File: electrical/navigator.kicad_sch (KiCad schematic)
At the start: 7 parts

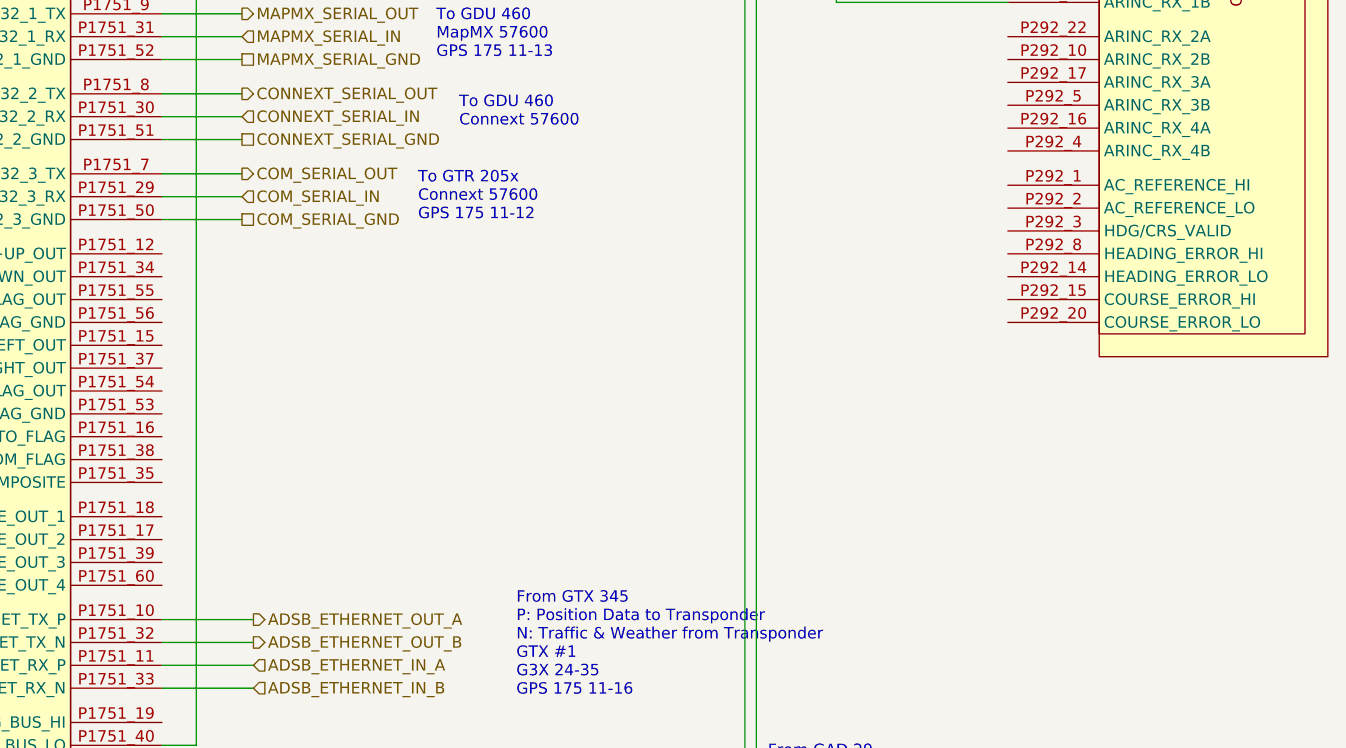
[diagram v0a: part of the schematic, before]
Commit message: Changed GPS 175 to not have connection to GTS 205x per g3xpert. Moved ELT GPS from GPS 175 and used RS-232 on GDU 460 for GEA 24 backup.
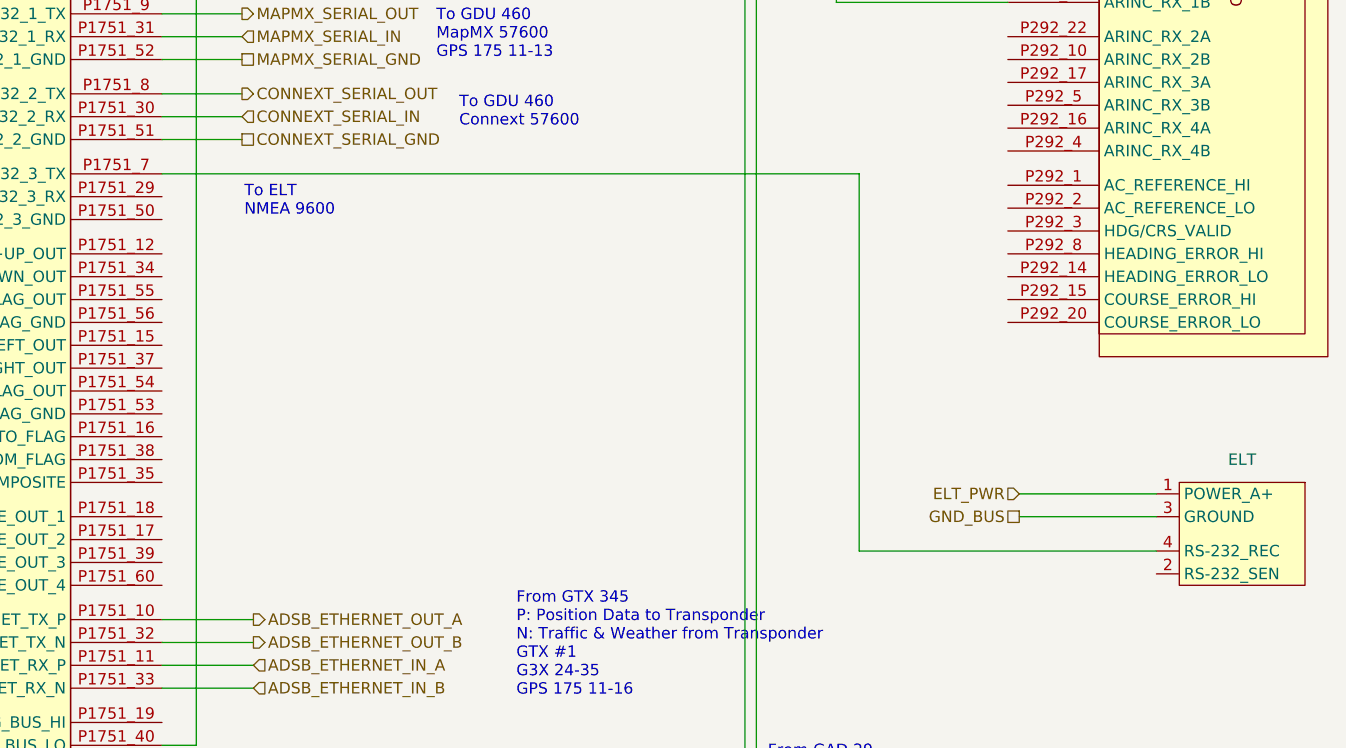
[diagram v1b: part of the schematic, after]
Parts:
- added ELT: ~, symbol flyerx:ACK_E-04
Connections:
- net GND: now also ELT.3 (GROUND)
- net COM_SERIAL_GND: no longer names the net of GPS175.P1751_50 (RS-232_3_GND)
- net COM_SERIAL_IN: no longer names the net of GPS175.P1751_29 (RS-232_3_RX)
- net COM_SERIAL_OUT: no longer names the net of GPS175.P1751_7 (RS-232_3_TX)
- net COM_SERIAL_OUT: now also ELT.4 (RS-232_REC)
- new net ELT_PWR: ELT.1 (POWER_A+)
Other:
- note added: "To ELT NMEA 9600"
- note removed: "To GTR 205x Connext 57600 GPS 175 11-12"
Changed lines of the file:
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@@
 	(paper "USLetter" portrait)
 	(title_block
-		(date "2025-09-08")
-		(rev "1.0")
+		(date "2025-09-09")
+		(rev "1.0.1")
 		(company "N78HR")
 	)
@@
 		)
 	)
+	(text "To ELT\nNMEA 9600"
+		(exclude_from_sim no)
+		(at 73.914 97.536 0)
+		(effects
+			(font
+				(size 1.27 1.27)
+			)
+			(justify left bottom)
+		)
+	)
 	(text "From GAD 29\nEFIS/AirData Low Gama Format 1\nG3X 24-38\nGPS 175 11-13"
 		(exclude_from_sim no)
 		(at 132.08 163.83 0)
-		(effects
-			(font
-				(size 1.27 1.27)
-			)
-			(justify left bottom)
-		)
-	)
-	(text "To GTR 205x\nConnext 57600\nGPS 175 11-12"
-		(exclude_from_sim no)
-		(at 93.218 98.044 0)
 		(effects
 			(font
@@
 	(wire
 		(pts
-			(xy 64.77 92.71) (xy 73.66 92.71)
-		)
-		(stroke
-			(width 0)
-			(type default)
-		)
-	)
-	(wire
-		(pts
 			(xy 64.77 156.21) (xy 68.58 156.21)
 		)
@@
 	(wire
 		(pts
+			(xy 64.77 92.71) (xy 142.24 92.71)
+		)
+		(stroke
+			(width 0)
+			(type default)
+		)
+	)
+	(wire
+		(pts
 			(xy 129.54 43.18) (xy 152.4 43.18)
 		)
@@
 	(wire
 		(pts
+			(xy 160.02 130.81) (xy 175.26 130.81)
+		)
+		(stroke
+			(width 0)
+			(type default)
+		)
+	)
+	(wire
+		(pts
 			(xy 31.75 260.35) (xy 36.83 260.35)
 		)
@@
 	(wire
 		(pts
+			(xy 160.02 128.27) (xy 175.26 128.27)
+		)
+		(stroke
+			(width 0)
+			(type default)
+		)
+	)
+	(wire
+		(pts
 			(xy 129.54 160.02) (xy 129.54 48.26)
 		)
@@
 	(wire
 		(pts
-			(xy 64.77 95.25) (xy 73.66 95.25)
-		)
-		(stroke
-			(width 0)
-			(type default)
-		)
-	)
-	(wire
-		(pts
 			(xy 64.77 77.47) (xy 73.66 77.47)
 		)
@@
 	(wire
 		(pts
+			(xy 142.24 134.62) (xy 175.26 134.62)
+		)
+		(stroke
+			(width 0)
+			(type default)
+		)
+	)
+	(wire
+		(pts
 			(xy 68.58 29.21) (xy 68.58 26.67)
 		)
@@
 	(wire
 		(pts
-			(xy 64.77 97.79) (xy 73.66 97.79)
-		)
-		(stroke
-			(width 0)
-			(type default)
-		)
-	)
-	(wire
-		(pts
 			(xy 64.77 74.93) (xy 73.66 74.93)
 		)
@@
 		(pts
 			(xy 64.77 144.78) (xy 74.93 144.78)
+		)
+		(stroke
+			(width 0)
+			(type default)
+		)
+	)
+	(wire
+		(pts
+			(xy 142.24 92.71) (xy 142.24 134.62)
 		)
 		(stroke
@@
 		)
 	)
+	(hierarchical_label "ELT_PWR"
+		(shape input)
+		(at 160.02 128.27 180)
+		(effects
+			(font
+				(size 1.27 1.27)
+			)
+			(justify right)
+		)
+	)
 	(hierarchical_label "CAN_LO_OUT"
 		(shape output)
@@
 		)
 	)
-	(hierarchical_label "COM_SERIAL_IN"
-		(shape input)
-		(at 73.66 95.25 0)
-		(effects
-			(font
-				(size 1.27 1.27)
-			)
-			(justify left)
-		)
-	)
-	(hierarchical_label "COM_SERIAL_GND"
-		(shape passive)
-		(at 73.66 97.79 0)
-		(effects
-			(font
-				(size 1.27 1.27)
-			)
-			(justify left)
-		)
-	)
 	(hierarchical_label "CAN_HI_IN"
 		(shape input)
@@
 		)
 	)
-	(hierarchical_label "COM_SERIAL_OUT"
-		(shape output)
-		(at 73.66 92.71 0)
-		(effects
-			(font
-				(size 1.27 1.27)
-			)
-			(justify left)
+	(hierarchical_label "GND_BUS"
+		(shape passive)
+		(at 160.02 130.81 180)
+		(effects
+			(font
+				(size 1.27 1.27)
+			)
+			(justify right)
 		)
 	)
@@
 					(unit 1)
 				)
+			)
+		)
+	)
+	(symbol
+		(lib_id "flyerx:ACK_E-04")
+		(at 191.77 127 0)
+		(mirror y)
+		(unit 1)
+		(exclude_from_sim no)
+		(in_bom yes)
+		(on_board yes)
+		(dnp no)
+		(property "Reference" "ELT"
+			(at 184.785 124.46 0)
+			(effects
+				(font
+					(size 1.27 1.27)
+				)
+			)
+		)
+		(property "Value" "~"
+			(at 191.77 125.73 0)
+			(effects
+				(font
+					(size 1.27 1.27)
+				)
+			)
+		)
+		(property "Footprint" ""
+			(at 191.77 125.73 0)
+			(effects
+				(font
+					(size 1.27 1.27)
+				)
+				(hide yes)
+			)
+		)
+		(property "Datasheet" ""
+			(at 191.77 125.73 0)
+			(effects
+				(font
+					(size 1.27 1.27)
+				)
+				(hide yes)
+			)
+		)
+		(property "Description" ""
+			(at 191.77 127 0)
+			(effects
+				(font
+					(size 1.27 1.27)
+				)
+			)
+		)
+		(pin "1"
+		)
+		(pin "2"
+		)
+		(pin "4"
+		)
+		(pin "3"
+		)
+		(instances
+			(project "electrical"
+				(path "/e8ec215a-dbe2-4eba-a577-e50a0a128049/a7d1a714-f940-4397-adef-d76b5058aa57"
+					(reference "ELT")
+					(unit 1)
+				)

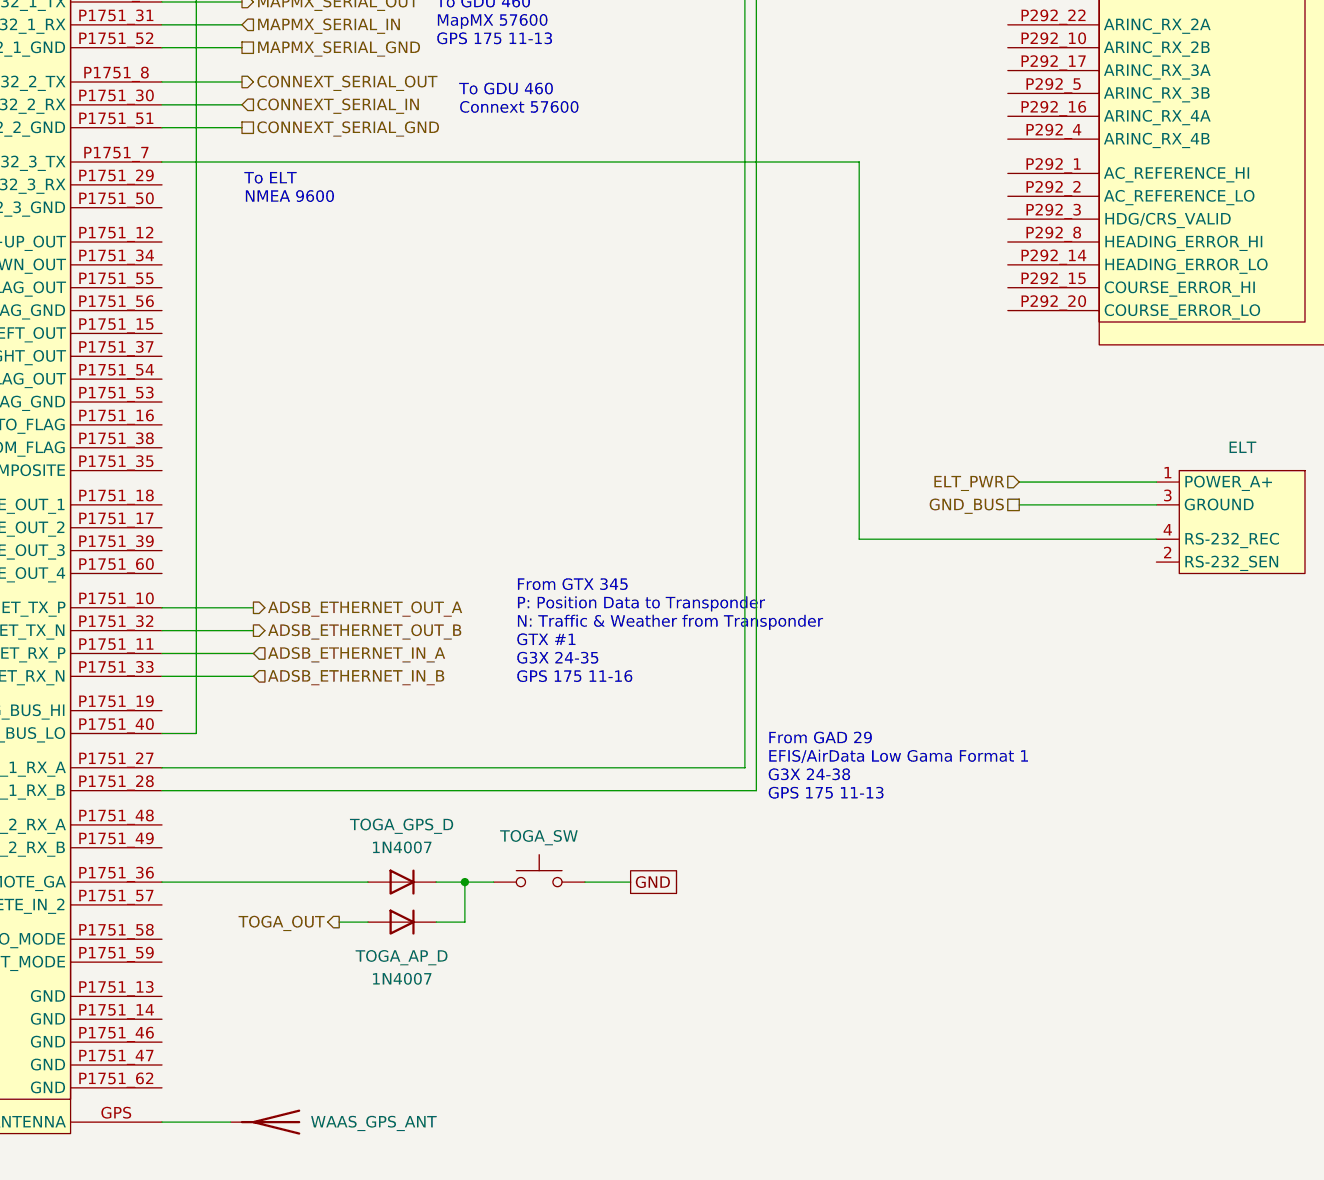
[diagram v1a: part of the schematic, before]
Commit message: Added connectors and non-CAN/RS232/Ethernet shields.
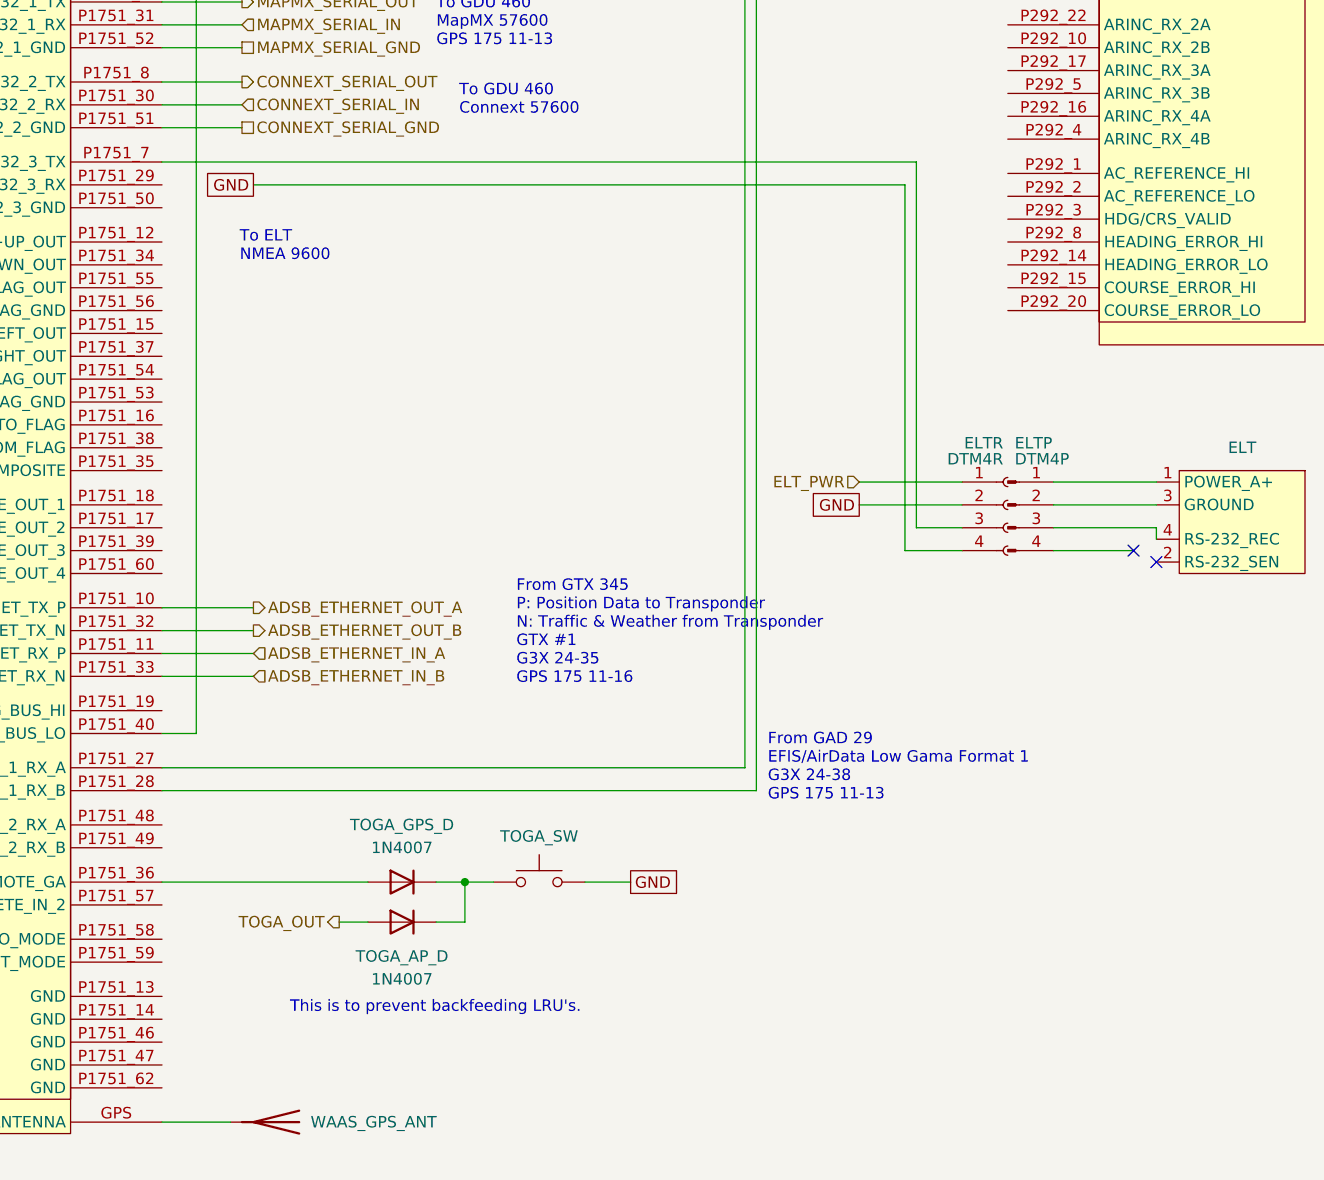
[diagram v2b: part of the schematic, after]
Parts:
- added ELTP: DTM4P, symbol Connector:Conn_01x04_Pin
- added ELTR: DTM4R, symbol Connector:Conn_01x04_Socket
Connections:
- net ELT_PWR: now also ELTR.1 (Pin_1); no longer ELT.1 (POWER_A+)
- net GND: now also ELTR.2 (Pin_2), ELTR.4 (Pin_4); no longer ELT.3 (GROUND)
- net at GPS175.P1751_7 (RS-232_3_TX): now also ELTR.3 (Pin_3); no longer ELT.4 (RS-232_REC)
- new net: ELT.1 (POWER_A+), ELTP.1 (Pin_1)
- new net: ELT.3 (GROUND), ELTP.2 (Pin_2)
- new net: ELT.4 (RS-232_REC), ELTP.3 (Pin_3)
- no-connect marks 2 -> 4
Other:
- note added: "This is to prevent backfeeding LRU's."
